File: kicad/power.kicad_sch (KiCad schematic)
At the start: 6 parts, among them J1 Bus_PCI_Express_x1, J201 USB_C_Receptacle_USB2.0_16P

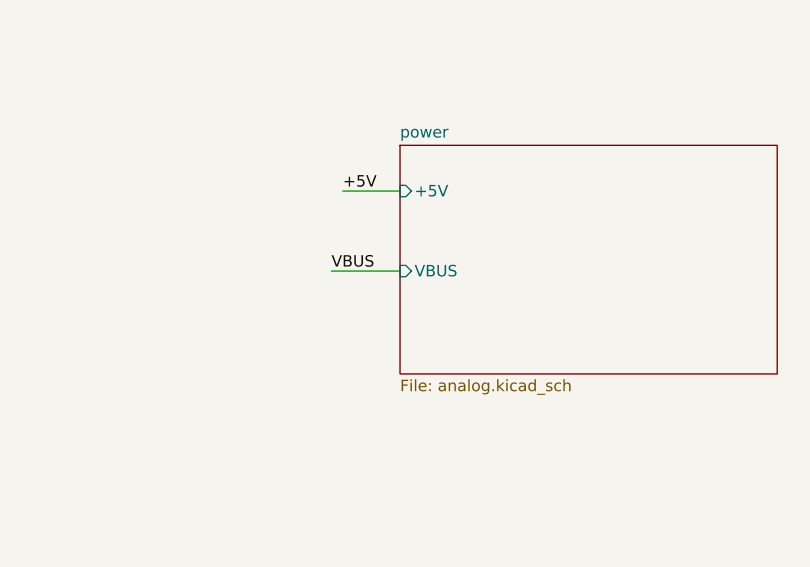
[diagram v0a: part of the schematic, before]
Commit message: add LCSC PNs and footprints for various components, import custom step file for inductor
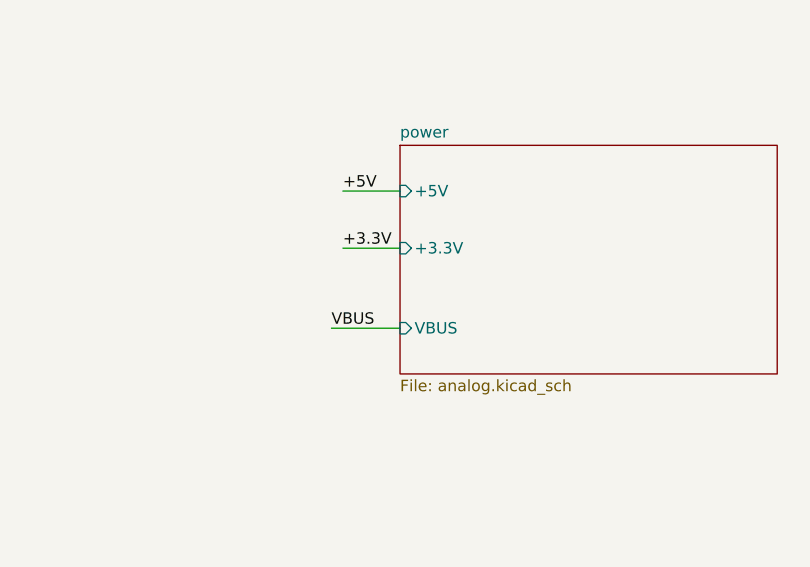
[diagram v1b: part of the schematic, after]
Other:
- sheet power ports: added +3.3V; removed none
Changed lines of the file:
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@@
+	(wire
+		(pts
+			(xy 182.88 81.28) (xy 189.23 81.28)
+		)
+		(stroke
+			(width 0)
+			(type default)
+		)
+	)
 	(wire
 		(pts
@@
 	(wire
 		(pts
-			(xy 181.61 83.82) (xy 189.23 83.82)
+			(xy 181.61 90.17) (xy 189.23 90.17)
 		)
 		(stroke
@@
 		)
 	)
+	(label "+3.3V"
+		(at 182.88 81.28 0)
+		(effects
+			(font
+				(size 1.27 1.27)
+			)
+			(justify left bottom)
+		)
+	)
 	(label "VBUS"
-		(at 181.61 83.82 0)
+		(at 181.61 90.17 0)
 		(effects
 			(font
@@
 			)
 		)
+		(property "DigiKey Link" ""
+			(at 63.5 45.72 90)
+			(effects
+				(font
+					(size 1.27 1.27)
+				)
+				(hide yes)
+			)
+		)
 		(pin "2"
 		)
@@
 			)
 		)
+		(property "DigiKey Link" ""
+			(at 105.41 81.28 0)
+			(effects
+				(font
+					(size 1.27 1.27)
+				)
+				(hide yes)
+			)
+		)
 		(pin "A3"
 		)
@@
 		)
 		(property "TYPE" ""
+			(at 63.5 43.18 90)
+			(effects
+				(font
+					(size 1.27 1.27)
+				)
+				(hide yes)
+			)
+		)
+		(property "DigiKey Link" ""
 			(at 63.5 43.18 90)
 			(effects
@@
 			)
 		)
+		(property "DigiKey Link" ""
+			(at 39.37 53.34 0)
+			(effects
+				(font
+					(size 1.27 1.27)
+				)
+				(hide yes)
+			)
+		)
 		(pin "B5"
 		)
@@
 			)
 		)
+		(property "DigiKey Link" ""
+			(at 157.48 149.86 0)
+			(effects
+				(font
+					(size 1.27 1.27)
+				)
+				(hide yes)
+			)
+		)
 		(pin "1"
 		)
@@
 			)
 		)
+		(property "DigiKey Link" ""
+			(at 157.48 142.24 0)
+			(effects
+				(font
+					(size 1.27 1.27)
+				)
+				(hide yes)
+			)
+		)
 		(pin "2"
 		)
@@
 		)
 		(pin "VBUS" input
-			(at 189.23 83.82 180)
+			(at 189.23 90.17 180)
 			(effects
 				(font
@@
 			(effects
 				(font
+					(size 1.27 1.27)
+				)
+				(justify left)
+			)
+		)
+		(pin "+3.3V" input
+			(at 189.23 81.28 180)
+			(effects
+				(font

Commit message: progress charging/balancing routing
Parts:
- renumbered R2 to R11
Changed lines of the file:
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@@
 		(on_board yes)
 		(dnp no)
-		(property "Reference" "R2"
+		(property "Reference" "R11"
 			(at 152.146 141.224 0)
 			(effects
@@
 			(project "recovery"
 				(path "/612ece3f-e722-4b33-8111-645d24cfcf05"
-					(reference "R2")
+					(reference "R11")
 					(unit 1)
 				)

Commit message: start via stitching
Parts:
- added D501: LED, LED_SMD:LED_0603_1608Metric, symbol Device:LED
- added R505: 1k, Resistor_SMD:R_0402_1005Metric, symbol Device:R
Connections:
- net +5V: now also R505.1
- net GND: now also D501.1 (K)
- new net: D501.2 (A), R505.2
